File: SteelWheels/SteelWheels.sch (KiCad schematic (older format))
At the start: 0 parts

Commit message: Completed SteelWheels
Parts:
- added P1, P2, P3: CONN_1, ~, symbol CONN_1
- added T1: Throttle, ~, symbol CONN_3
- added T2: Neopixels, ~, symbol CONN_3
- added U1: ADAFRUIT_POWERBOOST_1000, ~, symbol ADAFRUIT_POWERBOOST_1000
- added U2: METROMINI, ~, symbol METROMINI
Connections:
- new net: T2.2 (PM), U2.8 (#6)
- new net +3.3V: P3.1, T1.1 (P1), U2.21 (Aref), U2.26 (3V)
- new net +5V: P2.1, T2.1 (P1), U1.8 (5V), U2.22 (Vin)
- new net GND: P1.1, T1.3 (P3), T2.3 (P3), U1.5 (GND), U1.7 (GND), U2.23 (GND), U2.24 (GND)
- new net ThrottleIn: T1.2 (PM), U2.20 (A0)
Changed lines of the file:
@@
 LIBS:feather_m0_express
 LIBS:metromini
+LIBS:adafruit_powerboost_500
+LIBS:SteelWheels-cache
 EELAYER 27 0
 EELAYER END
@@
 Sheet 1 1
 Title ""
-Date "22 oct 2018"
+Date "4 nov 2018"
 Rev ""
 Comp ""
@@
 Comment4 ""
 $EndDescr
+$Comp
+L METROMINI U2
+U 1 1 5BDEF827
+P 3800 2300
+F 0 "U2" H 3800 2200 60  0000 C CNN
+F 1 "METROMINI" H 3800 2400 60  0000 C CNN
+F 2 "~" H 3800 2300 60  0000 C CNN
+F 3 "~" H 3800 2300 60  0000 C CNN
+	1    3800 2300
+	0    1    1    0
+$EndComp
+$Comp
+L ADAFRUIT_POWERBOOST_1000 U1
+U 1 1 5BDEF841
+P 1150 2400
+F 0 "U1" H 1150 2250 60  0000 C CNN
+F 1 "ADAFRUIT_POWERBOOST_1000" H 1200 2550 60  0000 C CNN
+F 2 "~" H 1150 2400 60  0000 C CNN
+F 3 "~" H 1150 2400 60  0000 C CNN
+	1    1150 2400
+	0    1    1    0
+$EndComp
+$Comp
+L CONN_3 T1
+U 1 1 5BDEF860
+P 6100 1750
+F 0 "T1" V 6050 1750 50  0000 C CNN
+F 1 "Throttle" V 6150 1750 40  0000 C CNN
+F 2 "~" H 6100 1750 60  0000 C CNN
+F 3 "~" H 6100 1750 60  0000 C CNN
+	1    6100 1750
+	1    0    0    -1
+$EndComp
+$Comp
+L CONN_3 T2
+U 1 1 5BDEF86F
+P 6150 2700
+F 0 "T2" V 6100 2700 50  0000 C CNN
+F 1 "Neopixels" V 6200 2700 40  0000 C CNN
+F 2 "~" H 6150 2700 60  0000 C CNN
+F 3 "~" H 6150 2700 60  0000 C CNN
+	1    6150 2700
+	1    0    0    -1
+$EndComp
+Wire Wire Line
+	3350 1850 3100 1850
+Wire Wire Line
+	3100 1850 3100 2350
+Wire Wire Line
+	3100 2350 3350 2350
+Wire Wire Line
+	3350 2150 3350 2050
+Wire Wire Line
+	3350 2050 2000 2050
+Wire Wire Line
+	2000 2050 2000 2100
+Wire Wire Line
+	2000 2100 1900 2100
+Wire Wire Line
+	1900 2300 2050 2300
+Wire Wire Line
+	2050 2300 2050 2050
+Connection ~ 2050 2050
+Wire Wire Line
+	1900 2400 2900 2400
+Wire Wire Line
+	2900 2400 2900 2250
+Wire Wire Line
+	2900 2250 3350 2250
+$Comp
+L +5V #PWR01
+U 1 1 5BDEF8F8
+P 2400 2300
+F 0 "#PWR01" H 2400 2390 20  0001 C CNN
+F 1 "+5V" H 2400 2390 30  0000 C CNN
+F 2 "" H 2400 2300 60  0000 C CNN
+F 3 "" H 2400 2300 60  0000 C CNN
+	1    2400 2300
+	1    0    0    -1
+$EndComp
+Wire Wire Line
+	2400 2300 2400 2400
+Connection ~ 2400 2400
+$Comp
+L CONN_1 P2
+U 1 1 5BDEF93B
+P 2500 2550
+F 0 "P2" H 2580 2550 40  0000 L CNN
+F 1 "CONN_1" H 2500 2605 30  0001 C CNN
+F 2 "~" H 2500 2550 60  0000 C CNN
+F 3 "~" H 2500 2550 60  0000 C CNN
+	1    2500 2550
+	1    0    0    -1
+$EndComp
+Wire Wire Line
+	2350 2550 2350 2400
+Connection ~ 2350 2400
+$Comp
+L CONN_1 P1
+U 1 1 5BDEF95A
+P 2300 1800
+F 0 "P1" H 2380 1800 40  0000 L CNN
+F 1 "CONN_1" H 2300 1855 30  0001 C CNN
+F 2 "~" H 2300 1800 60  0000 C CNN
+F 3 "~" H 2300 1800 60  0000 C CNN
+	1    2300 1800
+	1    0    0    -1
+$EndComp
+Wire Wire Line
+	2150 1800 2150 2050
+Connection ~ 2150 2050
+$Comp
+L CONN_1 P3
+U 1 1 5BDEF97B
+P 3000 1650
+F 0 "P3" H 3080 1650 40  0000 L CNN
+F 1 "CONN_1" H 3000 1705 30  0001 C CNN
+F 2 "~" H 3000 1650 60  0000 C CNN
+F 3 "~" H 3000 1650 60  0000 C CNN
+	1    3000 1650
+	-1   0    0    1
+$EndComp
+Wire Wire Line
+	3150 1650 3150 1850
+Connection ~ 3150 1850
+$Comp
+L GND #PWR02
+U 1 1 5BDEF99E
+P 2650 2150
+F 0 "#PWR02" H 2650 2150 30  0001 C CNN
+F 1 "GND" H 2650 2080 30  0001 C CNN
+F 2 "" H 2650 2150 60  0000 C CNN
+F 3 "" H 2650 2150 60  0000 C CNN
+	1    2650 2150
+	1    0    0    -1
+$EndComp
+Wire Wire Line
+	2650 2150 2650 2050
+Connection ~ 2650 2050
+$Comp
+L +3.3V #PWR03
+U 1 1 5BDEF9C3
+P 3250 1700
+F 0 "#PWR03" H 3250 1660 30  0001 C CNN
+F 1 "+3.3V" H 3250 1810 30  0000 C CNN
+F 2 "" H 3250 1700 60  0000 C CNN
+F 3 "" H 3250 1700 60  0000 C CNN
+	1    3250 1700
+	1    0    0    -1
+$EndComp
+Wire Wire Line
+	3250 1700 3250 1850
+Connection ~ 3250 1850
+$Comp
+L +3.3V #PWR04
+U 1 1 5BDEF9EA
+P 5750 1500
+F 0 "#PWR04" H 5750 1460 30  0001 C CNN
+F 1 "+3.3V" H 5750 1610 30  0000 C CNN
+F 2 "" H 5750 1500 60  0000 C CNN
+F 3 "" H 5750 1500 60  0000 C CNN
+	1    5750 1500
+	1    0    0    -1
+$EndComp
+Wire Wire Line
+	5750 1500 5750 1650
+$Comp
+L GND #PWR05
+U 1 1 5BDEFA13
+P 5750 1950
+F 0 "#PWR05" H 5750 1950 30  0001 C CNN
+F 1 "GND" H 5750 1880 30  0001 C CNN
+F 2 "" H 5750 1950 60  0000 C CNN
+F 3 "" H 5750 1950 60  0000 C CNN
+	1    5750 1950
+	1    0    0    -1
+$EndComp
+Wire Wire Line
+	5750 1850 5750 1950
+Text Label 3350 2450 2    60   ~ 0
+ThrottleIn
+Text Label 5750 1750 2    60   ~ 0
+ThrottleIn
+$Comp
+L +5V #PWR06
+U 1 1 5BDEFA3D
+P 5800 2450
+F 0 "#PWR06" H 5800 2540 20  0001 C CNN
+F 1 "+5V" H 5800 2540 30  0000 C CNN
+F 2 "" H 5800 2450 60  0000 C CNN
+F 3 "" H 5800 2450 60  0000 C CNN
+	1    5800 2450
+	1    0    0    -1
+$EndComp
+$Comp
+L GND #PWR07
+U 1 1 5BDEFA4C
+P 5800 2950
+F 0 "#PWR07" H 5800 2950 30  0001 C CNN
+F 1 "GND" H 5800 2880 30  0001 C CNN
+F 2 "" H 5800 2950 60  0000 C CNN
+F 3 "" H 5800 2950 60  0000 C CNN
+	1    5800 2950
+	1    0    0    -1
+$EndComp
+Wire Wire Line
+	5800 2600 5800 2450
+Wire Wire Line
+	5800 2800 5800 2950
+Wire Wire Line
+	4250 2350 5350 2350
+Wire Wire Line
+	5350 2350 5350 2700
+Wire Wire Line
+	5350 2700 5800 2700
 $EndSCHEMATC

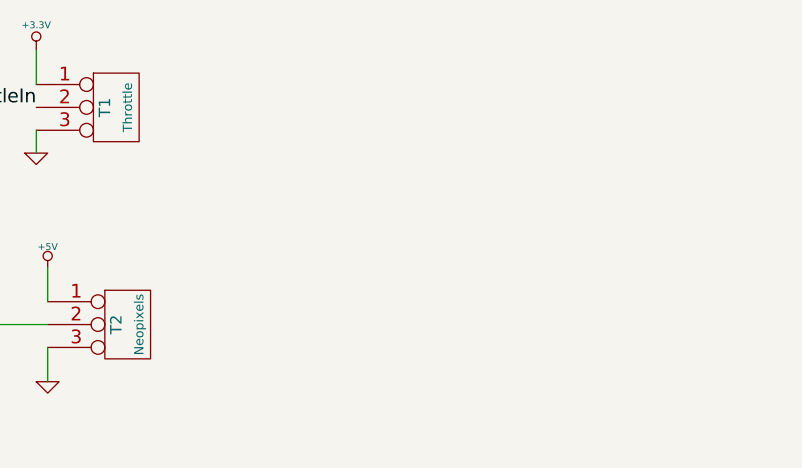
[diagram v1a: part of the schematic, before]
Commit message: Add detailed comments to both the code and the schematics
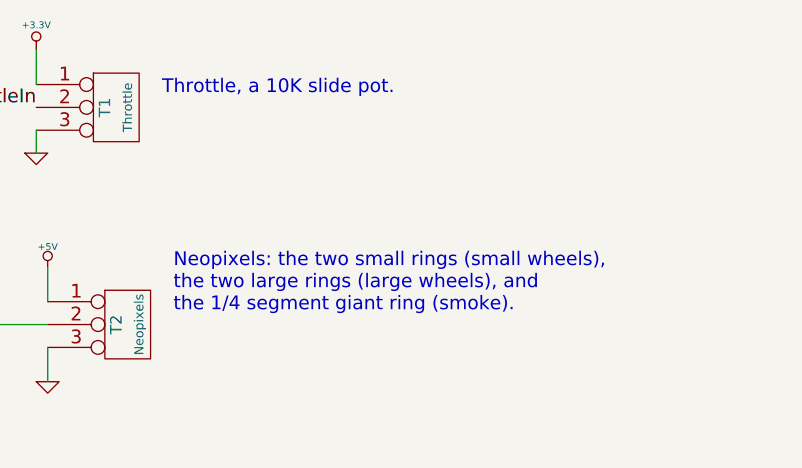
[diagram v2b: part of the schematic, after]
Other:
- note added: "Neopixels: the two small rings (small wheels), \nthe two large rings (large wheels), and \nthe 1/4 segment giant ring (smoke)."
- note added: "Throttle, a 10K slide pot."
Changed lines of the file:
@@
 Sheet 1 1
 Title ""
-Date "4 nov 2018"
+Date "11 nov 2018"
 Rev ""
 Comp ""
@@
 Wire Wire Line
 	5350 2700 5800 2700
+Text Notes 6300 1700 0    60   ~ 0
+Throttle, a 10K slide pot.
+Text Notes 6350 2650 0    60   ~ 0
+Neopixels: the two small rings (small wheels), \nthe two large rings (large wheels), and \nthe 1/4 segment giant ring (smoke).
 $EndSCHEMATC
